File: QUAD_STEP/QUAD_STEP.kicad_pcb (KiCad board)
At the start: 4 copper layers, 200 x 100 mm, 298 parts, among them J1 DB25_Female_LCNC, J10 ENC_HEADER, J11 ENC_HEADER, J12 PSoC_PROG, J13 POWER, J14 SCREW TERM, J15 SCREW TERM, J16 ENC_HEADER, J17 ENC_HEADER, J18 SCREW TERM, J19 SCREW TERM, J2 SCREW_TERM, J20 CYP_I2C, J3 USB_B, J4 SPARE_IN, J5 SPARE_OUT, J6 PROG_V, J7 RUN_V, J8 ICSP, J9 GPIO_header, Q1 BUK9K45-100E,115, Q10 BUK9K45-100E,115, Q11 BUK9K45-100E,115, Q12 BUK9K45-100E,115, Q13 BUK9K45-100E,115, Q14 BUK9K45-100E,115, Q15 BUK9K45-100E,115, Q16 BUK9K45-100E,115, Q2 BUK9K45-100E,115, Q3 BUK9K45-100E,115, Q4 BUK9K45-100E,115, Q5 BUK9K45-100E,115, Q6 BUK9K45-100E,115, Q7 BUK9K45-100E,115, Q8 BUK9K45-100E,115, Q9 BUK9K45-100E,115, U1 ATTINY841-SSU, U2 CY8C5468AXI-LP106, U3 TMC5160-TA, U4 TMC5160-TA, U5 TMC5160-TA, U6 TMC5160-TA, Y1 10MHz

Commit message: changed scope to 5 axis, preliminary completion of component positioning
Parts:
- removed J13: POWER, Connector_PinHeader_2.54mm:PinHeader_1x06_P2.54mm_Vertical
- removed R1, R2, R6, R7, R8, R9: 0R, Resistor_SMD:R_0603_1608Metric_Pad1.05x0.95mm_HandSolder
- added C100: 470n, Capacitor_SMD:C_0603_1608Metric, B.Cu at (80.0, 133.7)
- added C84: 100n, Capacitor_SMD:C_0603_1608Metric_Pad1.05x0.95mm_HandSolder, F.Cu at (109.2, 110.8)
- added C85: 2u2, Capacitor_SMD:C_0603_1608Metric_Pad1.05x0.95mm_HandSolder, F.Cu at (120.6, 119.7)
- added C86: 2u2, Capacitor_SMD:C_0603_1608Metric_Pad1.05x0.95mm_HandSolder, B.Cu at (120.6, 119.7)
- added C87: 470n, Capacitor_SMD:C_0603_1608Metric_Pad1.05x0.95mm_HandSolder, F.Cu at (100.3, 119.7)
- added C88: 150u 80V, CUSTOM_FP:CAPAE1350X1400N_EEVFK1J151Q, F.Cu at (138.4, 138.8)
- added C89: 10u, Capacitor_SMD:C_1210_3225Metric_Pad1.42x2.65mm_HandSolder, B.Cu at (142.2, 138.8)
- added C90: 10u, Capacitor_SMD:C_1210_3225Metric_Pad1.42x2.65mm_HandSolder, B.Cu at (134.6, 138.8)
- added C91: 100n, Capacitor_SMD:C_0603_1608Metric, B.Cu at (86.3, 133.7)
- added C92: 100n, Capacitor_SMD:C_0603_1608Metric, F.Cu at (99.0, 136.2)
- added C93: 100n, Capacitor_SMD:C_0603_1608Metric, B.Cu at (102.8, 119.7)
- added C94: 22n, Capacitor_SMD:C_0603_1608Metric, F.Cu at (102.8, 119.7)
- added C95: 220n, Capacitor_SMD:C_0603_1608Metric, F.Cu at (102.8, 136.2)
- added C96: 220n, Capacitor_SMD:C_0603_1608Metric, F.Cu at (96.5, 136.2)
- added C97: 470n, Capacitor_SMD:C_0603_1608Metric, F.Cu at (98.4, 129.9)
- added C98: 220n, Capacitor_SMD:C_0603_1608Metric, B.Cu at (86.3, 131.1)
- added C99: 220n, Capacitor_SMD:C_0603_1608Metric, B.Cu at (86.3, 137.5)
- added F5: BLADE_Fuse, CUSTOM_FP:keystone_3549_2_fuseholder_THT, F.Cu at (125.7, 136.2)
- added H1: MountingHole_Pad, MountingHole:MountingHole_4.5mm_Pad_Via, F.Cu at (50.8, 54.6)
- added H2: MountingHole_Pad, MountingHole:MountingHole_4.5mm_Pad_Via, F.Cu at (50.8, 144.6)
- added H3: MountingHole_Pad, MountingHole:MountingHole_4.5mm_Pad_Via, F.Cu at (240.8, 54.6)
- added H4: MountingHole_Pad, MountingHole:MountingHole_4.5mm_Pad_Via, F.Cu at (240.8, 144.6)
- added JP77: SolderJumper_2_Open, CUSTOM_FP:small_triangle_jumper, B.Cu at (61.6, 91.3)
- added JP78: SolderJumper_2_Open, CUSTOM_FP:small_triangle_jumper, B.Cu at (74.3, 102.7)
- added JP79: SolderJumper_2_Open, CUSTOM_FP:small_triangle_jumper, B.Cu at (81.9, 102.7)
- added JP80: SolderJumper_2_Open, CUSTOM_FP:small_triangle_jumper, F.Cu at (116.8, 108.3)
- added JP81: SolderJumper_2_Open, CUSTOM_FP:small_triangle_jumper, B.Cu at (116.8, 108.3)
- added JP82: SolderJumper_2_Open, CUSTOM_FP:small_triangle_jumper, F.Cu at (116.8, 110.8)
- added JP83: SolderJumper_2_Open, CUSTOM_FP:small_triangle_jumper, B.Cu at (116.8, 110.8)
- added JP84: SolderJumper_2_Open, CUSTOM_FP:small_triangle_jumper, F.Cu at (116.8, 105.7)
- added JP85: SolderJumper_2_Open, CUSTOM_FP:small_triangle_jumper, B.Cu at (116.8, 105.7)
- added JP86: SolderJumper_2_Open, CUSTOM_FP:small_triangle_jumper, F.Cu at (116.8, 103.2)
- added JP87: SolderJumper_2_Open, CUSTOM_FP:small_triangle_jumper, B.Cu at (116.8, 103.2)
- added JP88: SolderJumper_2_Open, CUSTOM_FP:small_triangle_jumper, F.Cu at (96.5, 122.3)
- added JP89: SolderJumper_2_Open, CUSTOM_FP:small_triangle_jumper, B.Cu at (96.5, 122.3)
- added JP90: SolderJumper_2_Open, CUSTOM_FP:small_triangle_jumper, F.Cu at (96.5, 119.7)
- added JP91: SolderJumper_2_Open, CUSTOM_FP:small_triangle_jumper, F.Cu at (116.8, 100.7)
- added JP92: SolderJumper_2_Open, CUSTOM_FP:small_triangle_jumper, B.Cu at (116.8, 100.7)
- added JP93: SolderJumper_2_Open, CUSTOM_FP:small_triangle_jumper, F.Cu at (109.2, 100.7)
- added JP94: SolderJumper_2_Open, CUSTOM_FP:small_triangle_jumper, B.Cu at (109.2, 100.7)
- added JP95: SolderJumper_2_Open, CUSTOM_FP:small_triangle_jumper, F.Cu at (102.8, 100.7)
- added JP96: SolderJumper_2_Open, CUSTOM_FP:small_triangle_jumper, F.Cu at (87.6, 115.2)
- added JP97: SolderJumper_2_Open, CUSTOM_FP:small_triangle_jumper, F.Cu at (96.5, 114.6)
- added JP98: SolderJumper_2_Open, CUSTOM_FP:small_triangle_jumper, F.Cu at (96.5, 117.2)
- added JP99: SolderJumper_2_Open, CUSTOM_FP:small_triangle_jumper, F.Cu at (136.4, 94.0)
- added Q17: BUK9K45-100E,115, CUSTOM_FP:TRANS_BUK7K12-60EX, B.Cu at (101.6, 136.0)
- added Q18: BUK9K45-100E,115, CUSTOM_FP:TRANS_BUK7K12-60EX, B.Cu at (95.2, 136.0)
- added Q19: BUK9K45-100E,115, CUSTOM_FP:TRANS_BUK7K12-60EX, F.Cu at (86.3, 129.9)
- added Q20: BUK9K45-100E,115, CUSTOM_FP:TRANS_BUK7K12-60EX, F.Cu at (86.3, 136.2)
- added R10: DNP, Resistor_SMD:R_0603_1608Metric_Pad1.05x0.95mm_HandSolder, F.Cu at (102.8, 108.3)
- added R11: 0R, Resistor_SMD:R_0603_1608Metric_Pad1.05x0.95mm_HandSolder, F.Cu at (102.8, 110.8)
- added R12: 2R2, Resistor_SMD:R_0603_1608Metric_Pad1.05x0.95mm_HandSolder, B.Cu at (109.2, 110.8)
- added R13: 22R, Resistor_SMD:R_0603_1608Metric_Pad1.05x0.95mm_HandSolder, F.Cu at (100.6, 129.9)
- added R14: 22R, Resistor_SMD:R_0603_1608Metric_Pad1.05x0.95mm_HandSolder, F.Cu at (102.8, 129.9)
- added R15: 47R, Resistor_SMD:R_0603_1608Metric_Pad1.05x0.95mm_HandSolder, F.Cu at (110.4, 133.7)
- added R16: 47R, Resistor_SMD:R_0603_1608Metric_Pad1.05x0.95mm_HandSolder, F.Cu at (110.4, 136.2)
- added R17: 0R022, CUSTOM_FP:WSH2818R0500FEA, B.Cu at (107.9, 135.0)
- added R18: 22R, Resistor_SMD:R_0603_1608Metric_Pad1.05x0.95mm_HandSolder, F.Cu at (93.9, 129.9)
- added R19: 22R, Resistor_SMD:R_0603_1608Metric_Pad1.05x0.95mm_HandSolder, F.Cu at (96.2, 129.9)
- added R20: 22R, Resistor_SMD:R_0603_1608Metric_Pad1.05x0.95mm_HandSolder, B.Cu at (80.0, 128.6)
- added R21: 22R, Resistor_SMD:R_0603_1608Metric_Pad1.05x0.95mm_HandSolder, B.Cu at (80.0, 131.1)
- added R22: 47R, Resistor_SMD:R_0603_1608Metric_Pad1.05x0.95mm_HandSolder, B.Cu at (85.0, 121.0)
- added R23: 47R, Resistor_SMD:R_0603_1608Metric_Pad1.05x0.95mm_HandSolder, B.Cu at (87.6, 121.0)
- added R24: 0R022, CUSTOM_FP:WSH2818R0500FEA, F.Cu at (86.3, 123.5)
- added R25: 22R, Resistor_SMD:R_0603_1608Metric_Pad1.05x0.95mm_HandSolder, B.Cu at (80.0, 136.2)
- added R26: 22R, Resistor_SMD:R_0603_1608Metric_Pad1.05x0.95mm_HandSolder, B.Cu at (80.0, 138.8)
- added TP6: CLK16, TestPoint:TestPoint_Pad_D1.0mm, F.Cu at (116.8, 113.4)
- added U7: TMC5160-TA, CUSTOM_FP:TMC5160-TA, F.Cu at (111.0, 119.4)
- C10, C11, C12, C13, C14, C15, C2, C34, C38, C39, C40, C42, C52, C55, C56, C58, C59, C64, C65, C66, C69, C72, C73, C74, C76, C8, C81, C82, C83, C9, JP40, JP42, JP44, JP46, JP48, JP50, JP52, JP54, JP56, JP59, JP62, JP64, JP66, JP68, R109, R128, R136, R137, R138, R139, R141, R142, R147, R155, R156, R157, R158, R160, R161, R162, R163: moved to B.Cu
- C20, C37, C54, C71: footprint CUSTOM:CAPAE1350X1400N_EEVFK1J151Q -> CUSTOM_FP:CAPAE1350X1400N_EEVFK1J151Q
- C5, C7: value 22p -> 18p; footprint Capacitor_SMD:C_0402_1005Metric -> Capacitor_SMD:C_0603_1608Metric_Pad1.05x0.95mm_HandSolder
- J2: value SCREW_TERM -> MTA-100; footprint CUSTOM:PHOENIX_1935161 -> CUSTOM_FP:640456-2
- J5: value SPARE_OUT -> ENC_HEADER; footprint Connector_PinHeader_2.54mm:PinHeader_1x03_P2.54mm_Vertical -> Connector_PinHeader_2.54mm:PinHeader_1x05_P2.54mm_Vertical
- J6: value PROG_V -> Conn_02x02_Odd_Even; footprint Connector_PinHeader_2.54mm:PinHeader_1x02_P2.54mm_Vertical -> Connector_PinHeader_2.54mm:PinHeader_2x02_P2.54mm_Vertical
- J7: value RUN_V -> CYP_GPIO; footprint Connector_PinHeader_2.54mm:PinHeader_1x02_P2.54mm_Vertical -> Connector_PinHeader_2.54mm:PinHeader_2x05_P2.54mm_Vertical
- J9: value GPIO_header -> SCREW TERM; footprint Connector_PinHeader_2.54mm:PinHeader_1x10_P2.54mm_Vertical -> CUSTOM_FP:CUI_TB002-500-06BE
- Q1, Q11, Q12, Q15, Q16, Q2, Q3, Q4, Q5, Q6, Q7, Q8: footprint CUSTOM:TRANS_BUK7K12-60EX -> CUSTOM_FP:TRANS_BUK7K12-60EX
- Q10, Q13, Q14, Q9: footprint CUSTOM:TRANS_BUK7K12-60EX -> CUSTOM_FP:TRANS_BUK7K12-60EX; moved to B.Cu
- R102, R114, R121, R140, R159, R95: footprint CUSTOM:WSH2818R0500FEA -> CUSTOM_FP:WSH2818R0500FEA
- R133, R152: footprint CUSTOM:WSH2818R0500FEA -> CUSTOM_FP:WSH2818R0500FEA; moved to B.Cu
- R4: value 0R -> DNP
- TP5: value ATM_SPARE -> PAR_SPARE; moved to B.Cu
- U3, U4, U5, U6: footprint CUSTOM:TMC5160-TA -> CUSTOM_FP:TMC5160-TA
- moved J11 342.8 mm to (192.9, 87.8), turned to 270 degrees
- moved R106 308.4 mm to (174.5, 92.7)
- moved R105 303.9 mm to (174.5, 95.2), turned to 180 degrees
- moved R107 303.4 mm to (174.5, 87.6), turned to 180 degrees
- moved C40 297.5 mm to (197.3, 64.8)
- moved R108 297.3 mm to (174.5, 90.2)
- moved R109 293.5 mm to (169.4, 87.6), turned to 180 degrees
- moved C33 291.9 mm to (169.4, 87.6), turned to 180 degrees
- moved C42 290.4 mm to (177.0, 77.5), turned to 90 degrees
- moved U4 290.0 mm to (168.1, 78.7)
- moved C43 289.8 mm to (177.0, 77.5), turned to 270 degrees
- moved C36 289.2 mm to (179.5, 77.5), turned to 90 degrees
- moved C3 288.1 mm to (61.6, 91.3), turned to 270 degrees
- moved C41 287.7 mm to (185.9, 62.2), turned to 270 degrees
- moved C34 287.6 mm to (157.9, 77.5), turned to 90 degrees
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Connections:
- J1 pad 14: Net-(J1-Pad14) -> /PAR_STEP5
- J1 pad 16: Net-(J1-Pad16) -> /PAR_DIR5
- J11 pad 4: /DRIVE_2/ENC_B -> /DRIVE_2/ENC_A
- J11 pad 5: /DRIVE_2/ENC_A -> /DRIVE_2/ENC_B
- J12 pad 1: /SWDIO -> /SWDCLK
- J12 pad 2: /SWDCLK -> /SWDIO
- J12 pad 4: GND -> /VTARG
- J12 pad 5: /VTARG -> GND
- J16 pad 4: /DRIVE_3/ENC_B -> /DRIVE_3/ENC_A
- J16 pad 5: /DRIVE_3/ENC_A -> /DRIVE_3/ENC_B
- J17 pad 4: /DRIVE_4/ENC_B -> /DRIVE_4/ENC_A
- J17 pad 5: /DRIVE_4/ENC_A -> /DRIVE_4/ENC_B
- J5 pad 1: Net-(J1-Pad17) -> GND
- J5 pad 2: Net-(J1-Pad16) -> Net-(J5-Pad2)
- J5 pad 3: Net-(J1-Pad14) -> /DRIVE_5/ENC_N
- J6 pad 1: Net-(J6-Pad1) -> /VTARG
- J6 pad 2: /VTARG -> Net-(J6-Pad2)
- J7 pad 1: Net-(J6-Pad1) -> Net-(J7-Pad1)
- J7 pad 2: /VCC_CONT -> Net-(J7-Pad2)
- J9 pad 1: Net-(J9-Pad1) -> Net-(F5-Pad3)
- J9 pad 2: Net-(J9-Pad2) -> GND
- J9 pad 3: Net-(J9-Pad3) -> /DRIVE_5/BMA1
- J9 pad 4: Net-(J9-Pad4) -> /DRIVE_5/BMA2
- J9 pad 5: Net-(J9-Pad5) -> /DRIVE_5/BMB1
- J9 pad 6: Net-(J9-Pad6) -> /DRIVE_5/BMB2
- R3 pad 1: /VDDA -> Net-(R3-Pad1)
- R3 pad 2: Net-(J6-Pad1) -> /DRIVE_5/VCC_IO
- R4 pad 1: /VDDD -> GND
- R4 pad 2: Net-(J6-Pad1) -> Net-(R3-Pad1)
- TP5 pad 1: Net-(TP5-Pad1) -> Net-(J1-Pad17)
- U1 pad 10: Net-(R9-Pad2) -> /ATM_CS4
- U1 pad 11: Net-(R8-Pad2) -> /ATM_CS3
- U1 pad 12: Net-(R7-Pad2) -> /ATM_CS2
- U1 pad 13: Net-(R6-Pad2) -> /ATM_CS1
- U1 pad 6: Net-(TP5-Pad1) -> /ATM_CS5
- U2 pad 22: Net-(J9-Pad1) -> Net-(J7-Pad1)
- U2 pad 23: Net-(J9-Pad2) -> Net-(J7-Pad2)
- U2 pad 24: Net-(J9-Pad3) -> Net-(J7-Pad3)
- U2 pad 25: Net-(J9-Pad4) -> Net-(J7-Pad4)
- U2 pad 27: Net-(J9-Pad5) -> Net-(J7-Pad5)
- U2 pad 28: Net-(J9-Pad6) -> Net-(J7-Pad6)
- U2 pad 31: Net-(J9-Pad7) -> Net-(J7-Pad7)
- U2 pad 32: Net-(J9-Pad8) -> Net-(J7-Pad8)
- U2 pad 33: Net-(J9-Pad9) -> Net-(J7-Pad9)
- U2 pad 34: Net-(J9-Pad10) -> Net-(J7-Pad10)
- U2 pad 44: Net-(U2-Pad44) -> /DIAG_1_5
- U2 pad 45: Net-(U2-Pad45) -> /DIAG_0_5
- U2 pad 46: Net-(U2-Pad46) -> /CYP_DIR5
- U2 pad 47: Net-(U2-Pad47) -> /CYP_STEP5
- U2 pad 48: Net-(U2-Pad48) -> /~CYP_ENA_5
- U2 pad 95: Net-(U2-Pad95) -> /CYP_CS5
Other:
- outline, holes or cut-outs redrawn
- board text added: "+"
- board text added: "-"
- board text added: "A"
- board text added: "A1"
- board text added: "A2"
- board text added: "B"
- board text added: "B1"
- board text added: "B2"
- board text added: "GND"
- board text added: "GPIO"
- board text added: "MISO"
- board text added: "MOSI"
- board text added: "N"
- board text added: "PROGRAMMER"
- board text added: "PSoC PROG"
- board text added: "RST"
- board text added: "SCK"
- board text added: "SCL"
- board text added: "SDA"
- board text added: "SPARE OUT"
- board text added: "SWDCLK"
- board text added: "SWDIO"
- board text added: "VCC"
- board text added: "VCC INTERNAL"
- board text added: "VTARG"

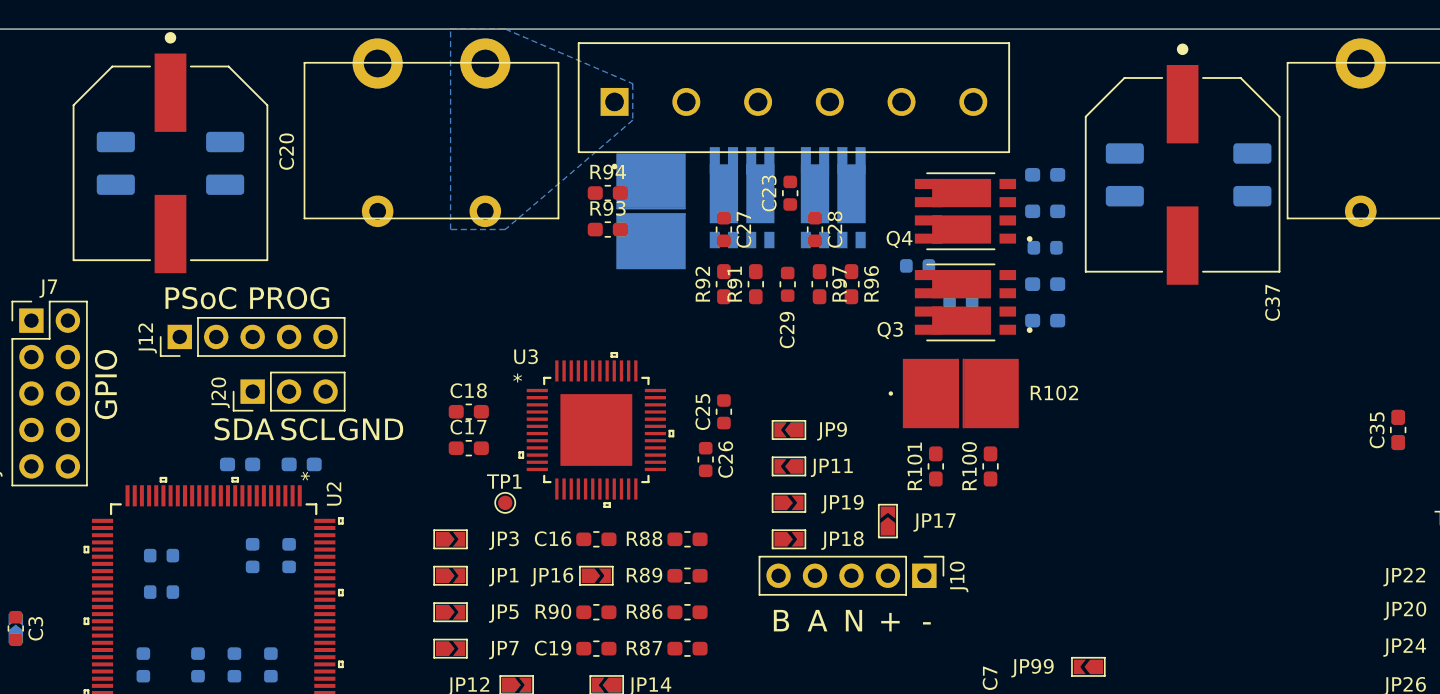
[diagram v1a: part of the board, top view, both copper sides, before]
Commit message: 3D links buggered, tinkered with alternate placement of FETs
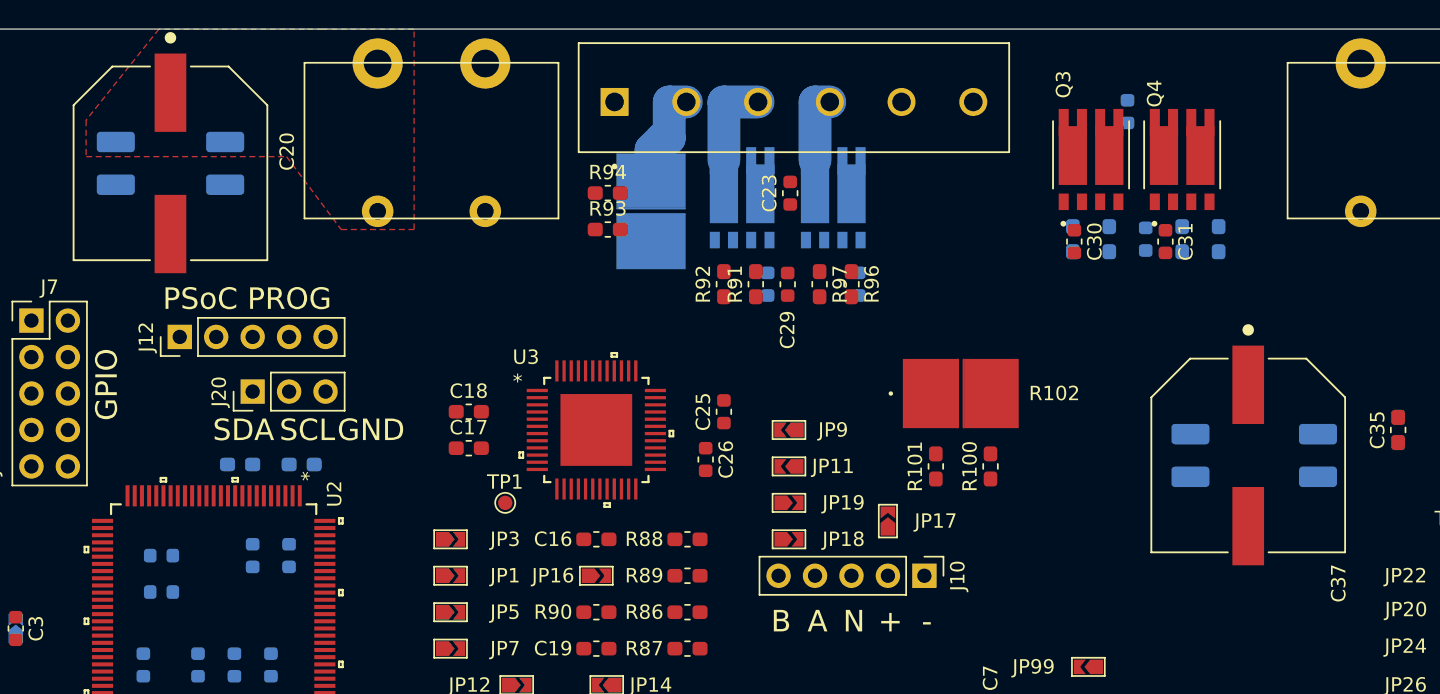
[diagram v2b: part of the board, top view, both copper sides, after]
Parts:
- C27, C28: moved to B.Cu
- C30, C31: moved to F.Cu
- moved C37 20.1 mm to (147.5, 79.2)
- moved C38 20.1 mm to (143.5, 79.2)
- moved C39 20.1 mm to (152.4, 79.2)
- moved C32 18.2 mm to (139.1, 55.3), turned to 90 degrees
- moved Q4 15.9 mm to (142.9, 58.3), turned to 90 degrees
- moved C31 14.7 mm to (141.7, 64.3), turned to 270 degrees
- moved Q3 13.7 mm to (136.5, 58.3), turned to 90 degrees
- moved R104 12.9 mm to (145.4, 64.2), turned to 270 degrees
- moved R103 9.74 mm to (142.9, 64.2), turned to 270 degrees
- moved C30 8.98 mm to (135.4, 64.3), turned to 270 degrees
- moved C24 7.03 mm to (140.4, 64.2), turned to 270 degrees
- moved R98 5.99 mm to (135.3, 64.2), turned to 90 degrees
- moved R99 5.46 mm to (137.8, 64.2), turned to 90 degrees
- moved C27 4.88 mm to (114.0, 67.3)
- moved C28 4.88 mm to (120.4, 67.3)
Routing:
- net /DRIVE_1/BMA1: track 0.00 -> 11.0 mm
- net /DRIVE_1/BMA2: track 0.00 -> 9.65 mm
- net GND: track 0.00 -> 7.47 mm
- added copper zone on F.Cu, net /DRIVE_1/VM
- added copper zone on POWER.Cu, net Net-(F1-Pad3)
- removed copper zone on B.Cu, net Net-(F1-Pad3)
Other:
- rule via_min_drill: 0.3 -> 0.254
- rule via_min_size: 0.4 -> 0.381
